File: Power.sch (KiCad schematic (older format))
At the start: 0 parts

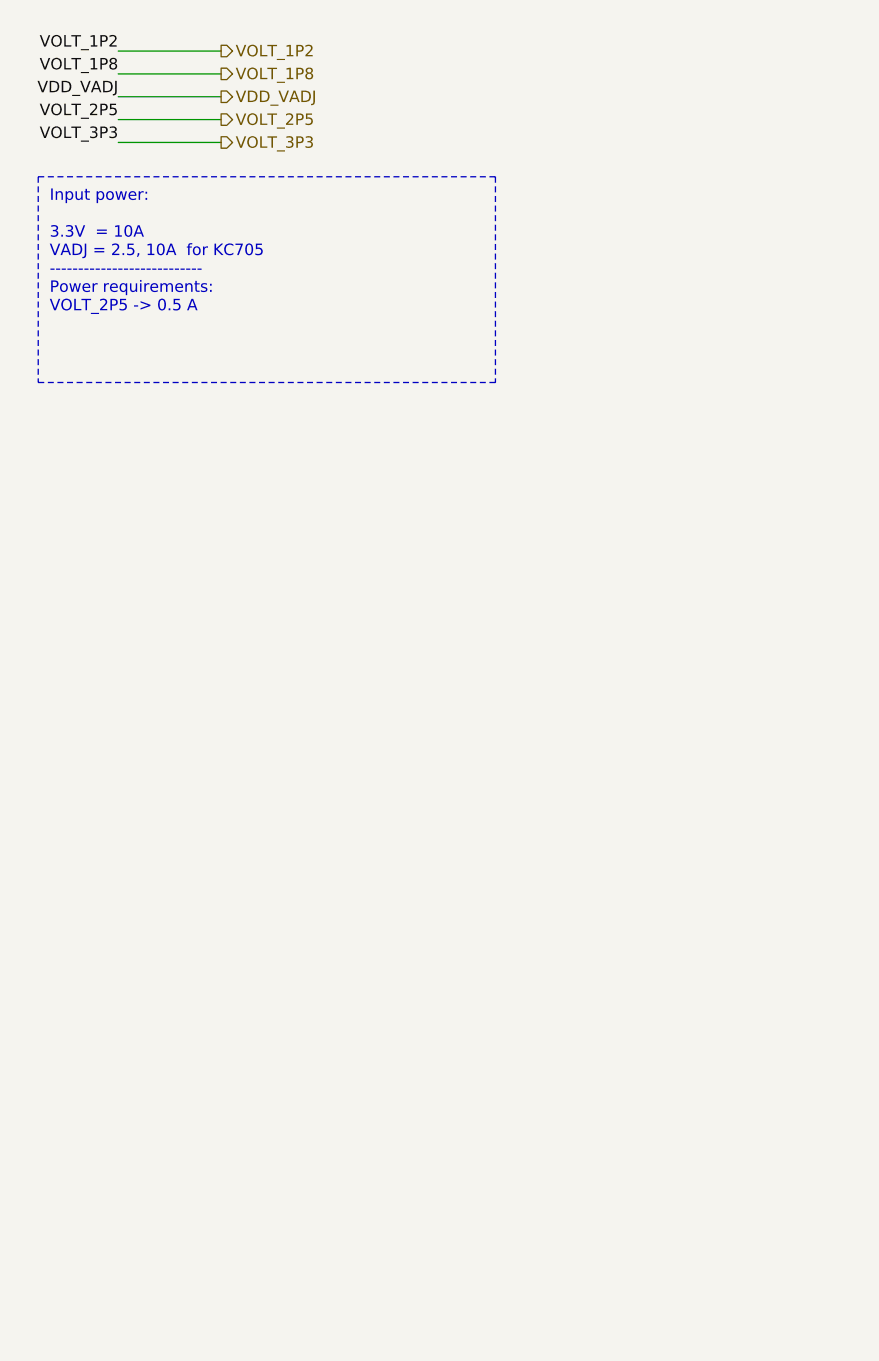
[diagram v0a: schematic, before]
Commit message: adding more power supplies
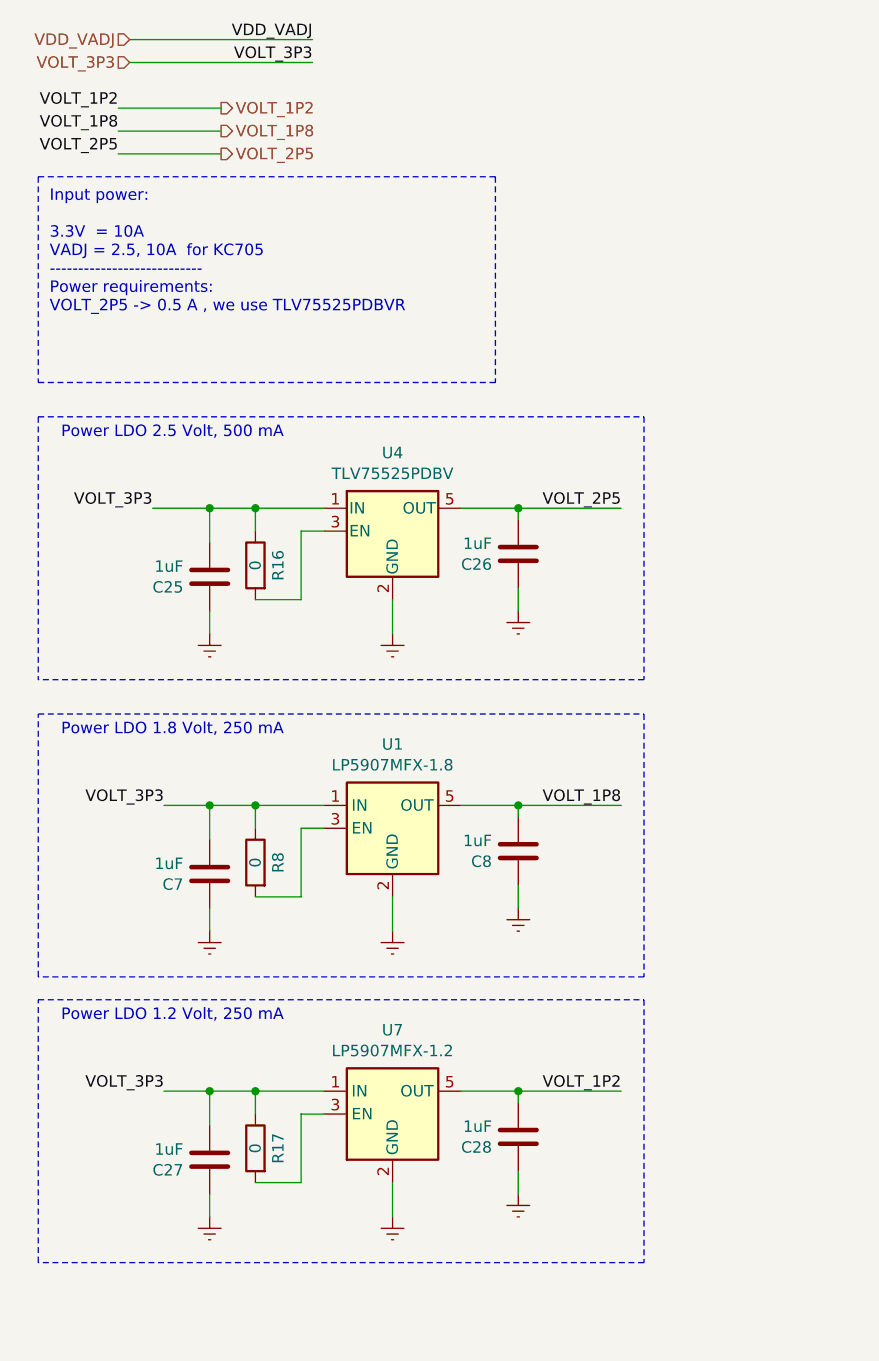
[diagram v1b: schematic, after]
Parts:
- added C25, C26, C27, C28, C7, C8: 1uF, Capacitors_SMD:C_0805, symbol FMC_MIPI_v2:C
- added R16, R17, R8: 0, Resistors_SMD:R_0805, symbol Device:R
- added U1: LP5907MFX-1.8, TO_SOT_Packages_SMD:SOT-23-5, symbol Regulator_Linear:LP5907MFX-1.8
- added U4: TLV75525PDBV, TO_SOT_Packages_SMD:SOT-23-5, symbol Regulator_Linear:TLV75525PDBV
- added U7: LP5907MFX-1.2, TO_SOT_Packages_SMD:SOT-23-5, symbol Regulator_Linear:LP5907MFX-1.2
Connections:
- net VOLT_1P2: now also C28.2, U7.5 (OUT)
- net VOLT_1P8: now also C8.2, U1.5 (OUT)
- net VOLT_2P5: now also C26.2, U4.5 (OUT)
- net VOLT_3P3: now also C25.2, C27.2, C7.2, R16.1, R17.1, R8.1, U1.1 (IN), U4.1 (IN), U7.1 (IN)
- new net: R16.2, U4.3 (EN)
- new net: R8.2, U1.3 (EN)
- new net: R17.2, U7.3 (EN)
- new net Earth: C25.1, C26.1, C27.1, C28.1, C7.1, C8.1, U1.2 (GND), U4.2 (GND), U7.2 (GND)
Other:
- note added: "Input power:\n\n3.3V = 10A\nVADJ = 2.5, 10A for KC705\n---------------------------\nPower requirements: \nVOLT_2P5 -> 0.5 A , we use TLV75525PDBVR\n"
- note added: "Power LDO 1.2 Volt, 250 mA"
- note added: "Power LDO 1.8 Volt, 250 mA"
- note added: "Power LDO 2.5 Volt, 500 mA"
- note removed: "Input power:\n\n3.3V = 10A\nVADJ = 2.5, 10A for KC705\n---------------------------\nPower requirements: \nVOLT_2P5 -> 0.5 A\n"

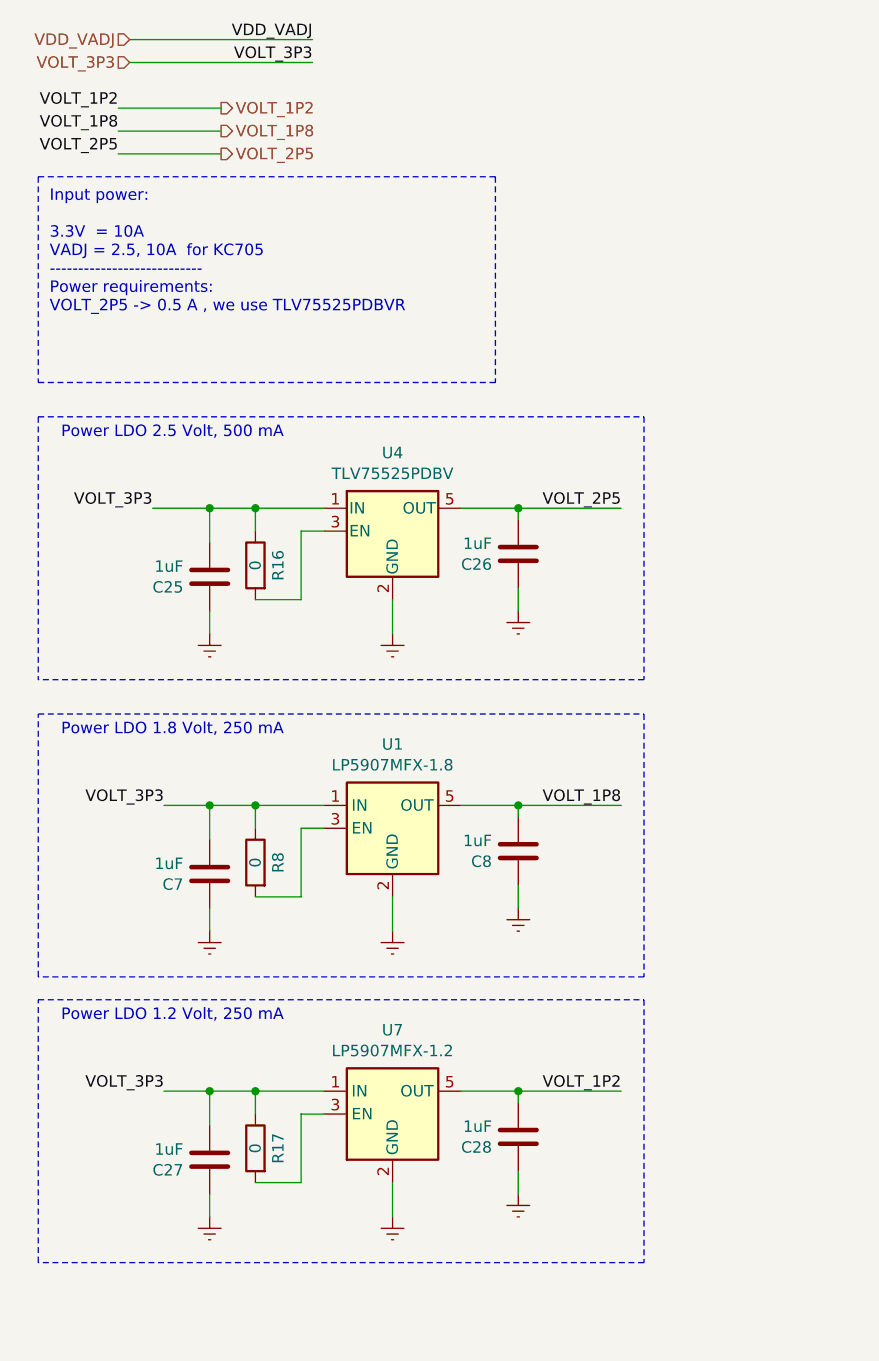
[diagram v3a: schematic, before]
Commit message: added 4 bit level shifter VADJ to 3.3 volt
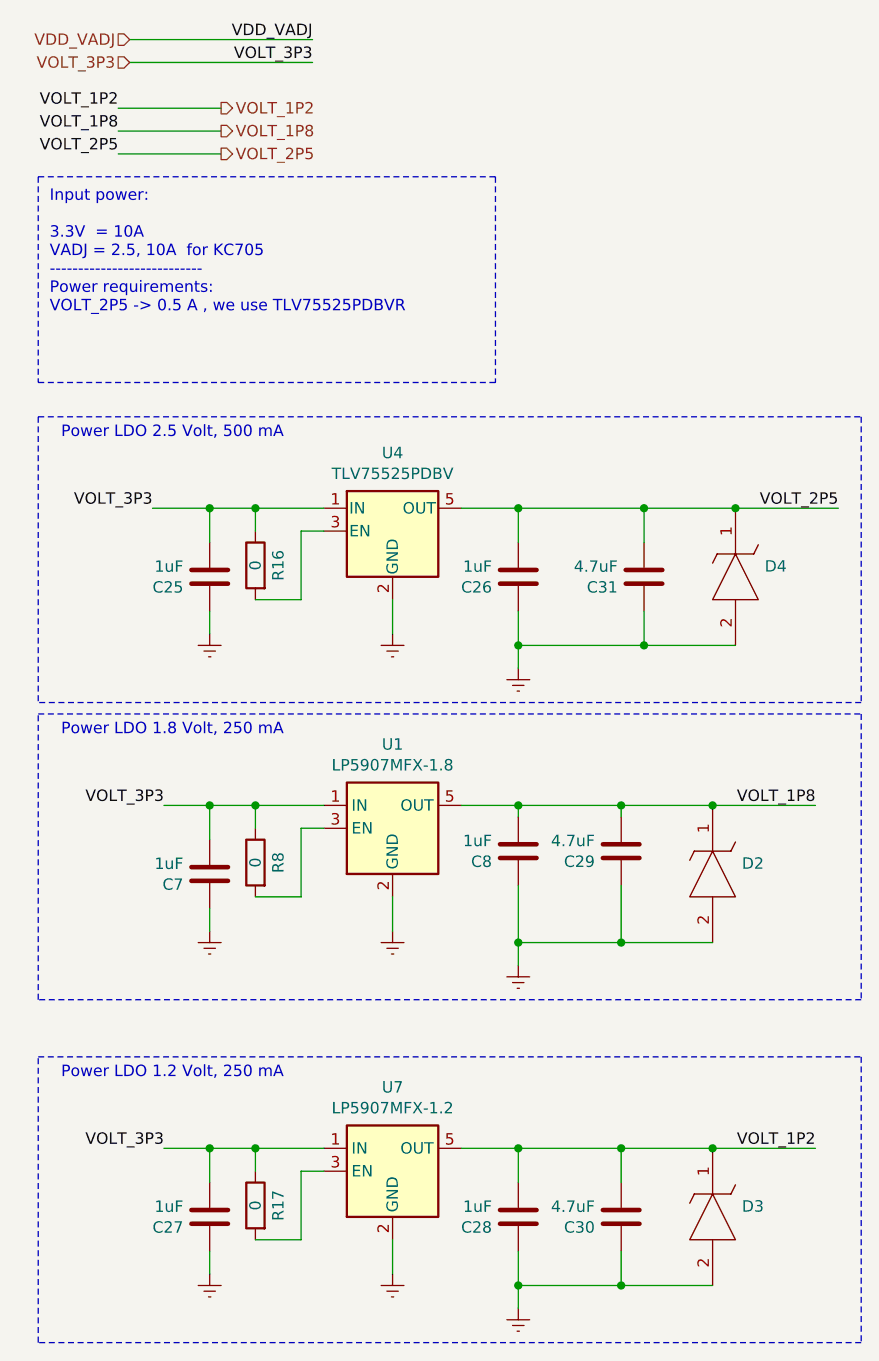
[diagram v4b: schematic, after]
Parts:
- added C29, C30, C31: 4.7uF, Capacitors_SMD:C_0805, symbol FMC_MIPI_v2:C
- added D2, D3, D4: UCLAMP0501H.TCT, Diodes_SMD:D_SOD-523, symbol FMC_MIPI_v2:UCLAMP0501H.TCT
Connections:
- net Earth: now also C29.1, C30.1, C31.1, D2.2, D3.2, D4.2
- net VOLT_1P2: now also C30.2, D3.1
- net VOLT_1P8: now also C29.2, D2.1
- net VOLT_2P5: now also C31.2, D4.1
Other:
- moved on the sheet: C26, C27, C28, R17, U7
